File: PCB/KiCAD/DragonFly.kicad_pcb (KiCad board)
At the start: 2 copper layers, 120 x 93 mm, 171 parts, among them CON1 AVR-ISP-6, J1 USB_OTG, J2 JACK_TRS_3pins, J3 MIC, J4 Conn_Coaxial, J5 Conn_Coaxial, J7 ANT, K1 TQ2-12VDC, P4 CONN_01X01, P5 CONN_01X01, P6 CONN_01X01, P7 CONN_01X01, Q1 MMBFJ310LT1G, Q10 MMBT4401LT1G, Q11 BFG591, Q2 MMBT2222A, Q3 SI2301-TP, Q4 SI2301-TP, Q5 MMBT2222A, Q6 MMBFJ310LT1G, Q7 IRF610, T1 1_9, T2 1_4, T3 1_4, T4 Transformer_1P_2S, T5 Transformer_1P_2S, U1 NE5532, U10 LD1117S33TR, U2 ATMEGA8-16AU, U3 ADuM1201CR, U4 LM78L06, U5 SA612, U6 FT232RL, U7 SI5351, U8 LM78L06, U9 SA612, Y1 8Mhz, Y10 8Mhz, Y2 8Mhz, Y3 8Mhz, Y4 8Mhz, Y5 8Mhz, Y6 8Mhz, Y7 8Mhz, Y8 27Mhz, Y9 8Mhz

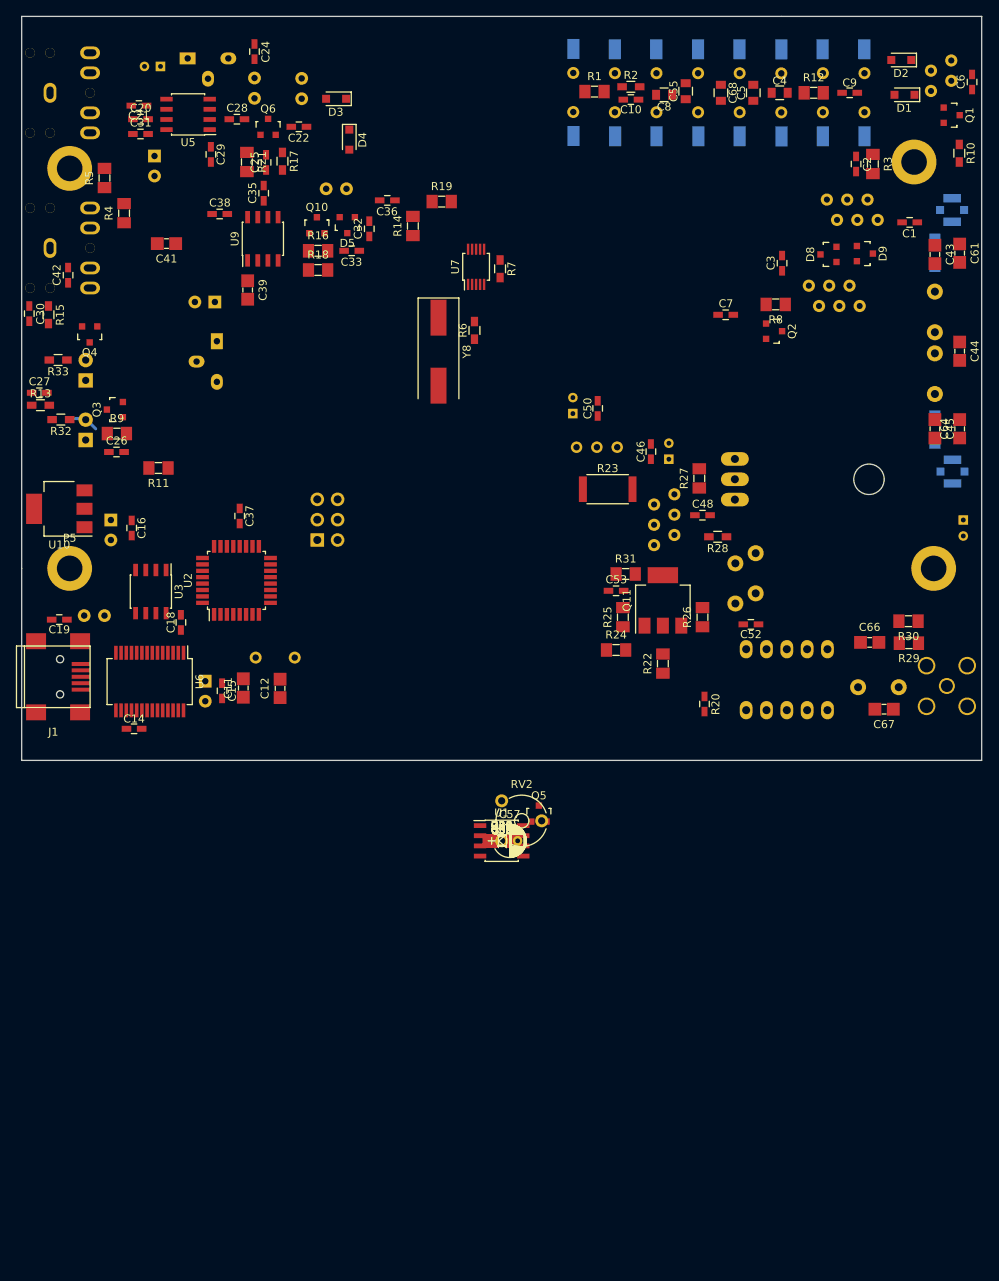
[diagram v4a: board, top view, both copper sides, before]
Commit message: PCB progress, IF TX, IF RX, PowerSupply Jack
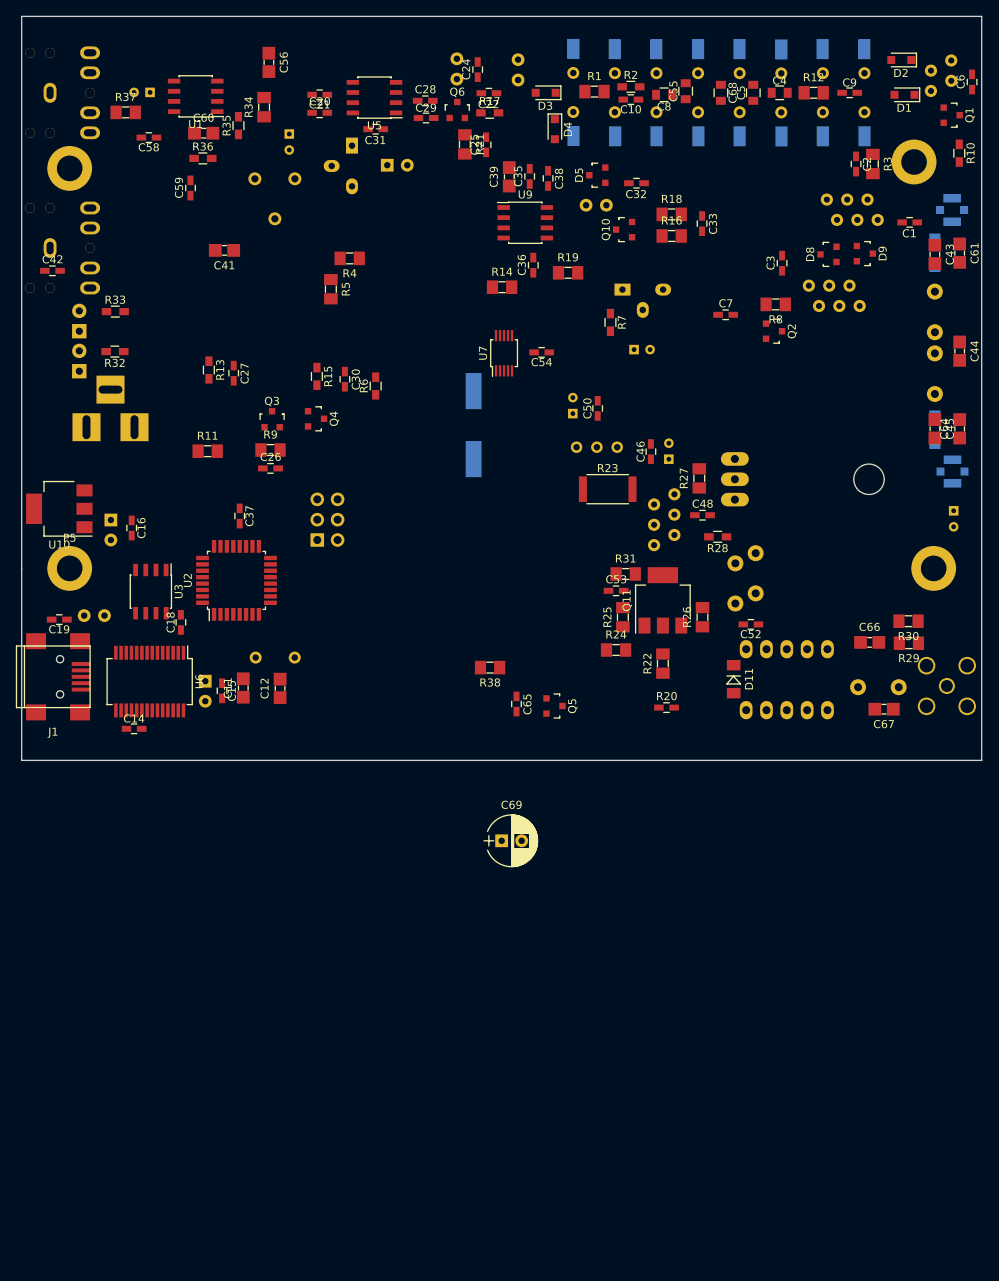
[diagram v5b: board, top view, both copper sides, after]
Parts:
- added C69: 220µF, DragonFly:CP_Radial_D6.3mm_P2.50mm, F.Cu at (95.0, 123.1)
- added CON2: BARREL_JACK, DragonFly:BARREL_JACK, B.Cu at (42.9, 71.3)
- C40: value 100µF -> 1µF; footprint DragonFly:CP_Radial_D6.3mm_P2.50mm -> DragonFly:CP_Radial_D4.0mm_P2.00mm
- C57, RV2, Y8: moved to B.Cu
- moved R37 102.5 mm to (48.0, 32.0)
- moved C56 101.6 mm to (65.9, 25.8), turned to 270 degrees
- moved U1 100.6 mm to (56.8, 30.0), turned to 180 degrees
- moved C58 98.3 mm to (50.9, 35.1), turned to 180 degrees
- moved R34 96.4 mm to (65.3, 31.4), turned to 90 degrees
- moved C60 96.0 mm to (57.8, 34.6)
- moved R35 95.3 mm to (62.1, 33.6), turned to 90 degrees
- moved R36 93.1 mm to (57.6, 37.8)
- moved C57 92.3 mm to (68.5, 34.7), turned to 270 degrees
- moved C59 90.4 mm to (56.1, 41.5), turned to 90 degrees
- moved RV2 86.7 mm to (69.2, 40.3), turned to 270 degrees
- moved C54 61.3 mm to (100.0, 62.0), turned to 180 degrees
- moved C40 52.7 mm to (111.5, 61.6), turned to 0 degrees
- moved U8 51.1 mm to (110.1, 54.1), turned to 0 degrees
- moved R18 44.7 mm to (116.2, 44.8)
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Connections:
- U7 pad 10: BFO_TX -> BFO_RX
- U7 pad 9: BFO_RX -> BFO_TX
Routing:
- net Net-(D6-Pad2): track 3.07 -> 0.00 mm

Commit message: PCB progress, add digital pin interface, polygon GND, some layout
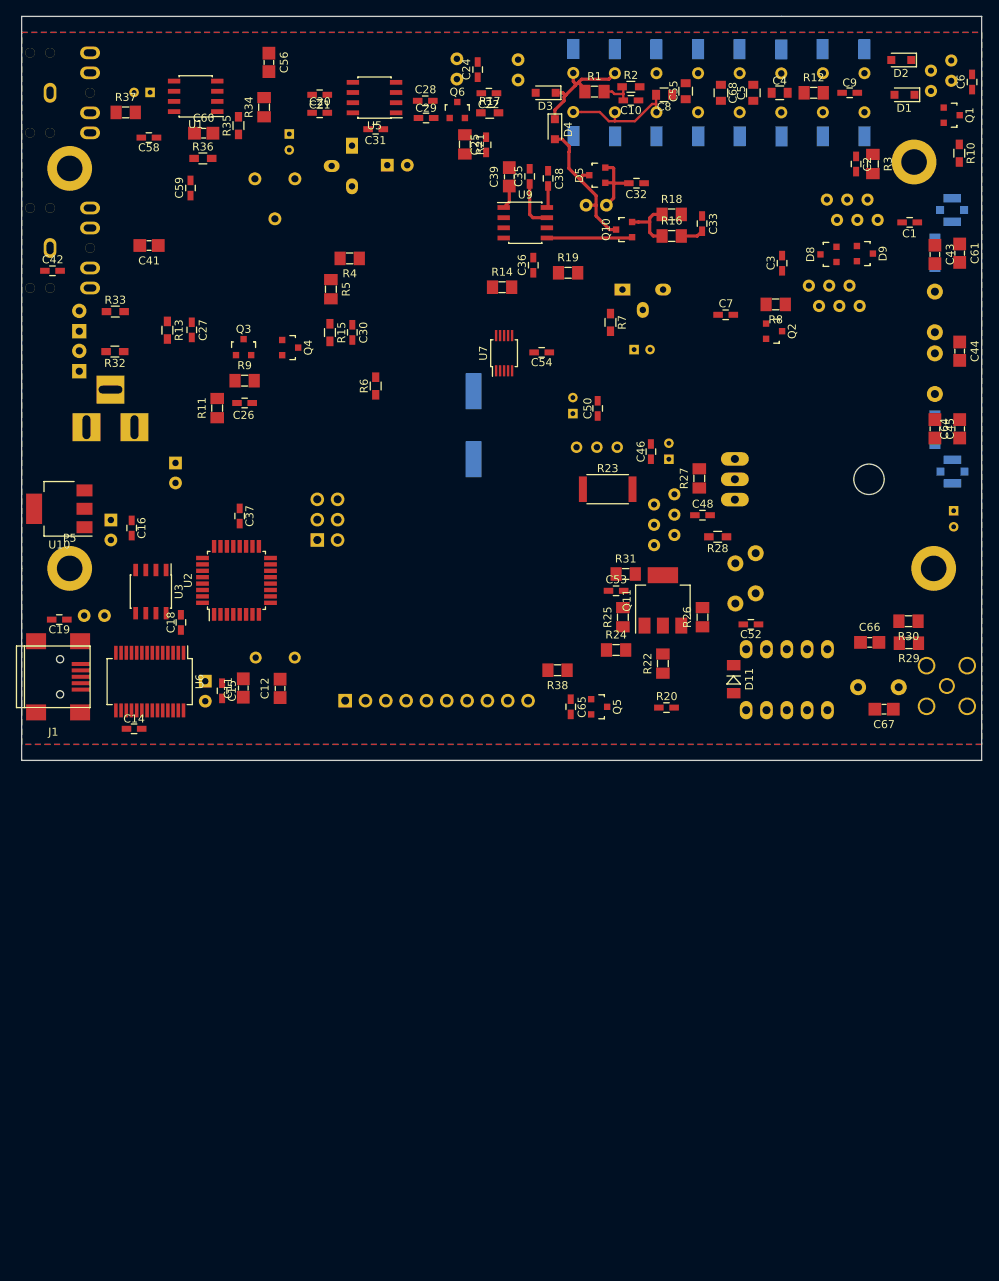
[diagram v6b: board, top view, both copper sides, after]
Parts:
- added J6: Conn_01x10, DragonFly:Pin_Header_Straight_1x10_Pitch2.54mm, B.Cu at (75.4, 105.5)
- C69: moved to B.Cu
- moved C69 62.4 mm to (54.2, 75.8), turned to 270 degrees
- moved Q3 9.69 mm to (62.7, 61.3)
- moved Q4 9.47 mm to (68.6, 61.4)
- moved C41 9.45 mm to (50.9, 48.6)
- moved R9 9.25 mm to (62.9, 65.5)
- moved C26 8.79 mm to (62.9, 68.3)
- moved R38 8.44 mm to (102.0, 101.7)
- moved C27 7.54 mm to (56.3, 59.2)
- moved R13 7.19 mm to (53.2, 59.2)
- moved C65 6.79 mm to (103.6, 106.3)
- moved C30 5.93 mm to (76.3, 59.5)
- moved R15 5.72 mm to (73.5, 59.5)
- moved Q5 5.59 mm to (107.2, 106.3)
- moved R11 5.52 mm to (59.4, 69.0), turned to 90 degrees
- moved C10 0.10 mm to (111.2, 30.5)
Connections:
- U2 pad 10: Net-(U2-Pad10) -> IO2
- U2 pad 11: Net-(U2-Pad11) -> IO3
- U2 pad 12: Net-(U2-Pad12) -> IO4
- U2 pad 13: Net-(U2-Pad13) -> IO5
- U2 pad 14: Net-(U2-Pad14) -> TX_PA
- U2 pad 9: Net-(U2-Pad9) -> IO1
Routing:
- net IF_TX: track 0.00 -> 18.4 mm
- net Net-(D3-Pad1): track 0.00 -> 15.4 mm
- net Net-(C8-Pad2): track 0.00 -> 15.0 mm
- net Net-(Q10-Pad1): track 0.00 -> 10.7 mm
- net TX_12V: track 0.00 -> 9.04 mm
- net Net-(Q10-Pad2): track 0.00 -> 7.47 mm
- net Net-(C35-Pad1): track 0.00 -> 6.12 mm
- net Net-(C10-Pad2): track 0.00 -> 4.29 mm
- net Net-(C39-Pad1): track 0.00 -> 2.98 mm
- net Net-(C33-Pad2): track 0.00 -> 2.85 mm
- net TX_6V: track 0.00 -> 2.75 mm
- added copper zone on B.Cu, net GND
- added copper zone on F.Cu, net GND
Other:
- net class Default: trace_width 0.4 -> 0.3

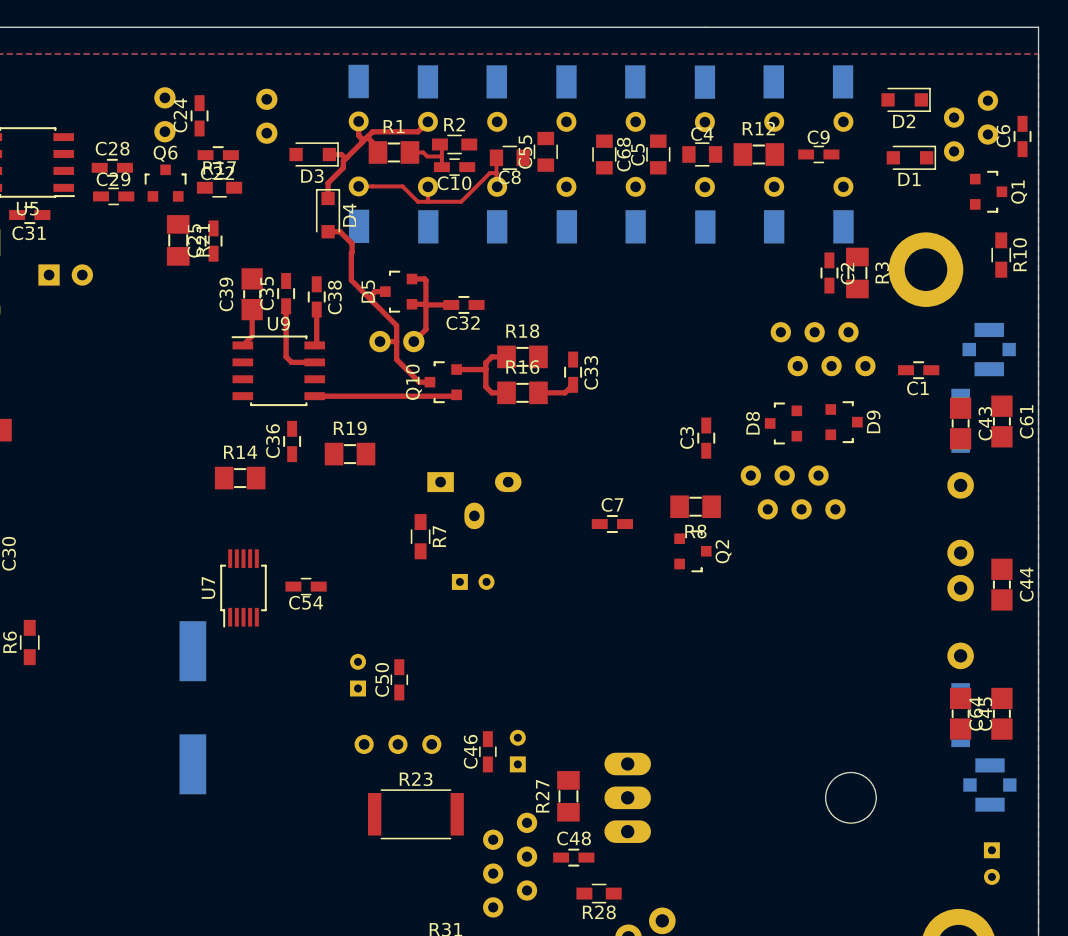
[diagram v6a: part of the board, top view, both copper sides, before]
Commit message: PCB progress, fix MMBFJ310 error
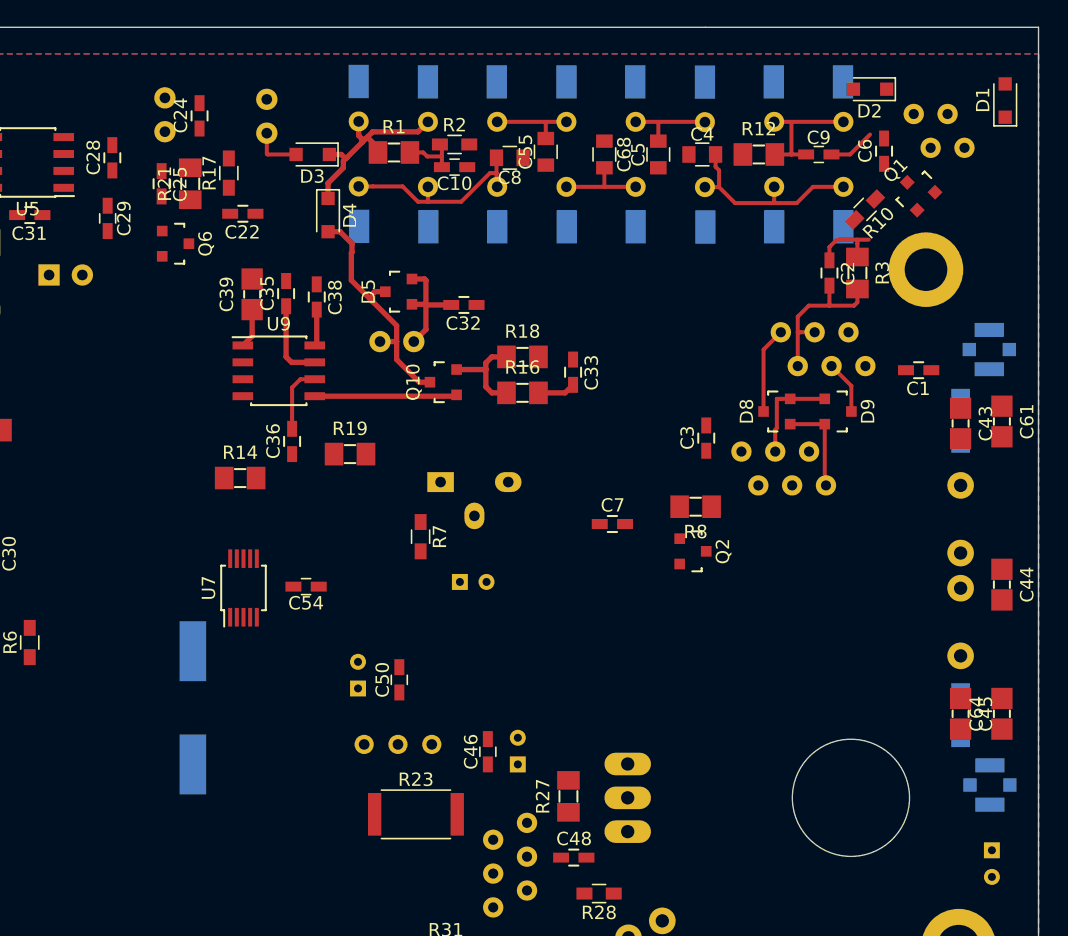
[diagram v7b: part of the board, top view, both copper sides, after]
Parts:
- Q6: value MMBFJ310LT1G -> MMBFJ310L
- Q7: footprint DragonFly:TO-220_Neutral123_Horizontal_LargePads -> DragonFly:TO-220_Neutral123_Horizontal_LargePads_BigHole
- moved R10 10.8 mm to (142.0, 33.7), turned to 225 degrees
- moved C6 10.5 mm to (143.4, 29.3)
- moved D1 8.34 mm to (152.5, 25.5), turned to 90 degrees
- moved C25 5.81 mm to (89.2, 31.8), turned to 270 degrees
- moved Q1 5.40 mm to (145.8, 32.4), turned to 45 degrees
- moved C22 4.77 mm to (95.2, 34.0)
- moved Q6 4.61 mm to (90.2, 36.2), turned to 270 degrees
- moved R21 4.34 mm to (91.3, 31.8), turned to 90 degrees
- moved D2 2.72 mm to (142.3, 24.6)
- moved T5 1.93 mm to (132.7, 51.9)
- moved C29 1.71 mm to (85.1, 34.4), turned to 270 degrees
- moved R17 1.30 mm to (94.2, 30.9), turned to 90 degrees
- moved D8 1.03 mm to (135.3, 48.9)
- moved D9 0.92 mm to (139.9, 48.9)
- moved T2 0.83 mm to (149.4, 29.1), turned to 180 degrees
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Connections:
- J1 pad 4: Net-(J1-Pad4) -> (no net)
- K1 pad 5: Net-(K1-Pad5) -> (no net)
- K1 pad 6: Net-(K1-Pad6) -> (no net)
- Q1 pad 1: Net-(D1-Pad1) -> Net-(C2-Pad1)
- Q1 pad 2: Net-(C2-Pad1) -> Net-(D1-Pad1)
- Q6 pad 1: Net-(C29-Pad2) -> Net-(C25-Pad2)
- Q6 pad 2: Net-(C25-Pad2) -> Net-(C29-Pad2)
- U2 pad 1: Net-(U2-Pad1) -> (no net)
- U2 pad 19: Net-(U2-Pad19) -> (no net)
- U2 pad 2: Net-(U2-Pad2) -> (no net)
- U2 pad 22: Net-(U2-Pad22) -> (no net)
- U2 pad 23: Net-(U2-Pad23) -> (no net)
- U2 pad 25: Net-(U2-Pad25) -> (no net)
- U2 pad 26: Net-(U2-Pad26) -> (no net)
- U2 pad 32: Net-(U2-Pad32) -> (no net)
- U5 pad 5: Net-(U5-Pad5) -> (no net)
- U6 pad 10: Net-(U6-Pad10) -> (no net)
- U6 pad 11: Net-(U6-Pad11) -> (no net)
- U6 pad 12: Net-(U6-Pad12) -> (no net)
- U6 pad 13: Net-(U6-Pad13) -> (no net)
- U6 pad 14: Net-(U6-Pad14) -> (no net)
- U6 pad 2: Net-(U6-Pad2) -> (no net)
- U6 pad 22: Net-(U6-Pad22) -> (no net)
- U6 pad 23: Net-(U6-Pad23) -> (no net)
- U6 pad 27: Net-(U6-Pad27) -> (no net)
- U6 pad 28: Net-(U6-Pad28) -> (no net)
- U6 pad 3: Net-(U6-Pad3) -> (no net)
- U6 pad 6: Net-(U6-Pad6) -> (no net)
- U6 pad 9: Net-(U6-Pad9) -> (no net)
- U9 pad 4: Net-(U9-Pad4) -> (no net)
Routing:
- net Net-(C4-Pad2): track 0.00 -> 15.2 mm
- net Net-(C2-Pad2): track 0.00 -> 12.4 mm
- net Net-(C9-Pad1): track 0.00 -> 10.0 mm
- net Net-(D8-Pad2): track 0.00 -> 7.61 mm
- net Net-(D8-Pad1): track 0.00 -> 7.24 mm
- net Net-(C5-Pad2): track 0.00 -> 6.66 mm
- net Net-(C68-Pad2): track 0.00 -> 6.63 mm
- net Net-(D8-Pad3): track 0.00 -> 6.49 mm
- net Net-(C55-Pad2): track 0.00 -> 6.47 mm
- net Net-(C2-Pad1): track 0.00 -> 5.48 mm
- net Net-(C36-Pad2): track 0.00 -> 5.05 mm
- net Net-(D9-Pad3): track 0.00 -> 4.03 mm
- net IF_RX: track 0.00 -> 3.77 mm
- net Net-(C9-Pad2): track 0.00 -> 3.52 mm

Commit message: mixer schema is done, pcb progress, fix 78l06 issue
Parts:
- removed D8, D9: BAT54S, DragonFly:SOT-23
- removed Q2: MMBT2222A, DragonFly:SOT-23
- added C70: 100nF, DragonFly:C_0603_HandSoldering, F.Cu at (134.7, 60.2)
- added C71: 100nF, DragonFly:C_0603_HandSoldering, F.Cu at (127.4, 60.2)
- added C72: 100µF, DragonFly:CP_Radial_D6.3mm_P2.50mm, B.Cu at (139.3, 58.9)
- added C73: 10nF, DragonFly:C_0603_HandSoldering, F.Cu at (145.1, 44.0)
- added R39: 1.5k, DragonFly:R_1206_0603, F.Cu at (134.8, 56.4)
- added R40: 3.3K, DragonFly:R_1206_0603, F.Cu at (124.1, 56.7)
- added U11: NC7SB3157, DragonFly:SOT-23-6, F.Cu at (134.7, 52.6)
- added U12: NC7SB3157, DragonFly:SOT-23-6, F.Cu at (127.5, 52.7)
- added U13: L78L06_TO92, DragonFly:TO-92_Molded_Wide_Oval, B.Cu at (136.6, 69.5)
- C1: value 100nF -> 10nF
- C7: value 10nF -> 10µF; footprint DragonFly:C_0603_HandSoldering -> DragonFly:CP_Radial_D4.0mm_P2.00mm; moved to B.Cu
- R8: value 150k -> 3.3K
- U4, U8: value LM78L06 -> L78L06_TO92
- moved C1 26.0 mm to (120.8, 52.1), turned to 0 degrees
- moved C3 13.8 mm to (123.8, 63.1), turned to 0 degrees
- moved C7 9.40 mm to (122.8, 66.7)
- moved T4 7.23 mm to (136.2, 41.1)
- moved R8 6.85 mm to (124.0, 60.4)
- moved T5 6.37 mm to (136.2, 46.5), turned to 180 degrees
- moved U8 2.86 mm to (108.4, 51.9)
- moved U4 0.11 mm to (76.2, 36.2)
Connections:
- C1 pad 1: BPF -> VFO
- C2 pad 2: Net-(C2-Pad2) -> IF
- C3 pad 1: +12V -> Net-(C3-Pad1)
- C7 pad 1: VFO -> Net-(C3-Pad1)
- C7 pad 2: Net-(C7-Pad2) -> GND
- R3 pad 2: Net-(C2-Pad2) -> IF
- R8 pad 1: Net-(Q2-Pad3) -> GND
- R8 pad 2: Net-(C7-Pad2) -> Net-(C3-Pad1)
- T4 pad 1: Net-(C1-Pad2) -> IF
- T4 pad 3: Net-(D9-Pad3) -> Net-(T4-Pad3)
- T4 pad 4: Net-(C2-Pad2) -> Net-(T4-Pad4)
- T4 pad 5: Net-(C2-Pad2) -> Net-(T4-Pad5)
- T4 pad 6: Net-(D8-Pad3) -> Net-(T4-Pad6)
- T5 pad 1: +12V -> Net-(C73-Pad1)
- T5 pad 2: Net-(Q2-Pad3) -> GND
- T5 pad 3: Net-(D8-Pad2) -> Net-(T4-Pad3)
- T5 pad 4: GND -> Net-(T4-Pad5)
- T5 pad 5: GND -> Net-(T4-Pad4)
- T5 pad 6: Net-(D8-Pad1) -> Net-(T4-Pad6)
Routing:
- net Net-(C2-Pad2): track 12.4 -> 0.00 mm
- net Net-(D8-Pad2): track 7.61 -> 0.00 mm
- net Net-(D8-Pad1): track 7.24 -> 0.00 mm
- net Net-(D8-Pad3): track 6.49 -> 0.00 mm
- net Net-(D9-Pad3): track 4.03 -> 0.00 mm
